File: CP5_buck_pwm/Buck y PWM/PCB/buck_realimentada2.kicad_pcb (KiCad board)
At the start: 2 copper layers, 95 x 89 mm, 52 parts, among them J1 Vin, J10 Conn_vcc, J11 Conn_vref, J12 Conn_vg1, J13 Conn_vg2, J14 Conn_cuadrada, J15 Conn_sampling, J2 Vout, J3 Conn_gnd, J4 Conn_error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

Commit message: Archivos de salida
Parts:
- moved J11 16.6 mm to (137.1, 137.5)
- moved J4 15.5 mm to (147.3, 139.7)
- moved J12 13.7 mm to (163.4, 91.2)
- moved C13 12.0 mm to (126.0, 76.0), turned to 180 degrees
- moved U4 9.27 mm to (119.9, 69.7), turned to 0 degrees
- moved Rc1 5.30 mm to (165.1, 127.0), turned to -90 degrees
- moved R16 4.27 mm to (160.2, 138.6)
- moved C1 2.92 mm to (157.2, 119.9)
- moved C3 2.92 mm to (157.3, 124.2)
- moved J15 2.34 mm to (177.0, 137.2)
- moved J10 1.17 mm to (152.8, 77.7)
- moved U5 0.59 mm to (129.6, 120.9)
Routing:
- net Net-(U4-ADJ): track 19.5 -> 33.9 mm
- net error: track 67.2 -> 75.3 mm
- net Vin: track 135.3 -> 143.3 mm
- net VCCPWM: track 157.3 -> 153.4 mm
- net Net-(C7-Pad2): track 15.2 -> 11.5 mm
- net sampling: track 24.8 -> 27.2 mm
- net Vref: track 40.4 -> 42.3 mm
- net Vout: track 38.5 -> 39.9 mm
- net Vg1: track 36.8 -> 38.0 mm

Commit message: PCB corregida
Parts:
- removed J5: Conn_pwm, Connector_PinHeader_2.54mm:PinHeader_1x01_P2.54mm_Vertical
- added J7: Conn_01x02_Pin, Connector_PinHeader_2.54mm:PinHeader_1x02_P2.54mm_Vertical, F.Cu at (126.0, 109.5)
- moved C12 10.6 mm to (123.2, 115.8), turned to 0 degrees
- moved C6 4.20 mm to (126.1, 88.8)
- moved J11 2.25 mm to (136.0, 139.5)
- moved U5 1.48 mm to (128.3, 120.2)
- moved U1 1.17 mm to (131.1, 110.1)
- moved R4 0.29 mm to (114.3, 90.2), turned to 0 degrees
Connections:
- C10 pad 2: Net-(U7A-+) -> Net-(U7A--)
- C6 pad 1: Net-(U6B-+) -> Net-(U6B--)
- C7 pad 1: Net-(U7A-+) -> Net-(U7A--)
- R1 pad 1: Net-(U6A--) -> Net-(U6A-+)
- R15 pad 1: Net-(U7A-+) -> Net-(U7A--)
- R17 pad 2: Net-(U7A-+) -> Net-(U7A--)
- R4 pad 2: Net-(U6B-+) -> Net-(U6B--)
- R6 pad 2: Net-(U6A--) -> Net-(U6A-+)
- U1 pad 2: pwm -> Net-(J7-Pin_1)
- U6 pad 2: Net-(U6A--) -> Net-(U2A--)
- U6 pad 3: Net-(U2A--) -> Net-(U6A-+)
- U6 pad 5: Net-(U6B-+) -> Net-(U2A--)
- U6 pad 6: Net-(U2A--) -> Net-(U6B--)
- U7 pad 2: Vref -> Net-(U7A--)
- U7 pad 3: Net-(U7A-+) -> Vref
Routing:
- net Net-(U7A-+): track 22.8 -> 0.00 mm
- net Net-(U7A--): track 0.00 -> 21.7 mm
- net Net-(U6B-+): track 18.0 -> 0.00 mm
- net Net-(U6B--): track 0.00 -> 13.3 mm
- net Net-(U6A--): track 12.3 -> 0.00 mm
- net Net-(U6A-+): track 0.00 -> 10.2 mm
- net Net-(J7-Pin_1): track 0.00 -> 6.43 mm
- net pwm: track 24.1 -> 19.2 mm
- net Net-(U2A--): track 44.1 -> 46.7 mm
- net Vref: track 42.3 -> 43.9 mm
- net Triangular: track 40.4 -> 38.7 mm
- net Net-(U1-VS): track 14.2 -> 12.6 mm
- net HO: track 3.82 -> 4.98 mm
- net Net-(D1-K): track 8.72 -> 9.71 mm
- net GND: track 0.00 -> 0.50 mm

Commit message: Add files via upload
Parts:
- added J5: Conn_gnd2, Connector_PinHeader_2.54mm:PinHeader_1x01_P2.54mm_Vertical, F.Cu at (104.9, 129.8)
- added J8: Conn_vd, Connector_PinHeader_2.54mm:PinHeader_1x01_P2.54mm_Vertical, F.Cu at (171.4, 63.5)
- R1, R10, R12, R15, R16, R17, R2, R3, R5, R7: footprint Resistor_THT:R_Axial_DIN0204_L3.6mm_D1.6mm_P5.08mm_Horizontal -> Resistor_THT:R_Axial_DIN0204_L3.6mm_D1.6mm_P7.62mm_Horizontal
- R4: footprint Resistor_THT:R_Axial_DIN0204_L3.6mm_D1.6mm_P5.08mm_Horizontal -> Potentiometer_THT:Potentiometer_Bourns_3296W_Vertical
- moved J10 21.4 mm to (133.6, 68.3)
- moved J12 19.6 mm to (150.2, 76.7)
- moved C8 11.6 mm to (109.6, 88.6), turned to 180 degrees
- moved J6 8.54 mm to (108.6, 115.5)
- moved M3 6.87 mm to (159.1, 105.8)
- moved J13 6.86 mm to (158.0, 112.2)
- moved C3 6.42 mm to (151.1, 122.6)
- moved C1 6.20 mm to (151.1, 118.9)
- moved Rc1 5.62 mm to (161.6, 122.6), turned to 0 degrees
- moved C5 5.40 mm to (139.7, 63.1), turned to 90 degrees
- moved R16 4.92 mm to (163.5, 142.3)
- moved J15 4.34 mm to (177.0, 141.5)
- moved C4 4.28 mm to (137.5, 101.2), turned to -90 degrees
- moved C13 4.20 mm to (122.5, 73.7), turned to -90 degrees
- moved J7 3.74 mm to (128.5, 112.3), turned to -90 degrees
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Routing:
- net Vd: track 32.1 -> 57.5 mm
- net Vg2: track 35.0 -> 13.2 mm
- net Vout: track 39.9 -> 55.9 mm
- net Net-(U2A--): track 46.7 -> 60.8 mm
- net Triangular: track 38.7 -> 43.8 mm
- net Net-(C7-Pad2): track 11.5 -> 15.8 mm
- net Vg1: track 38.0 -> 42.2 mm
- net VCCPWM: track 153.7 -> 156.6 mm
- net Net-(U6B--): track 13.3 -> 16.1 mm
- net Net-(D1-K): track 9.71 -> 12.1 mm
- net Net-(U1-VS): track 12.6 -> 10.7 mm
- net Net-(U7A--): track 21.7 -> 23.6 mm
- net LO: track 3.78 -> 5.57 mm
- net Net-(J7-Pin_1): track 6.43 -> 4.95 mm
- net Vin: track 143.3 -> 142.1 mm
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
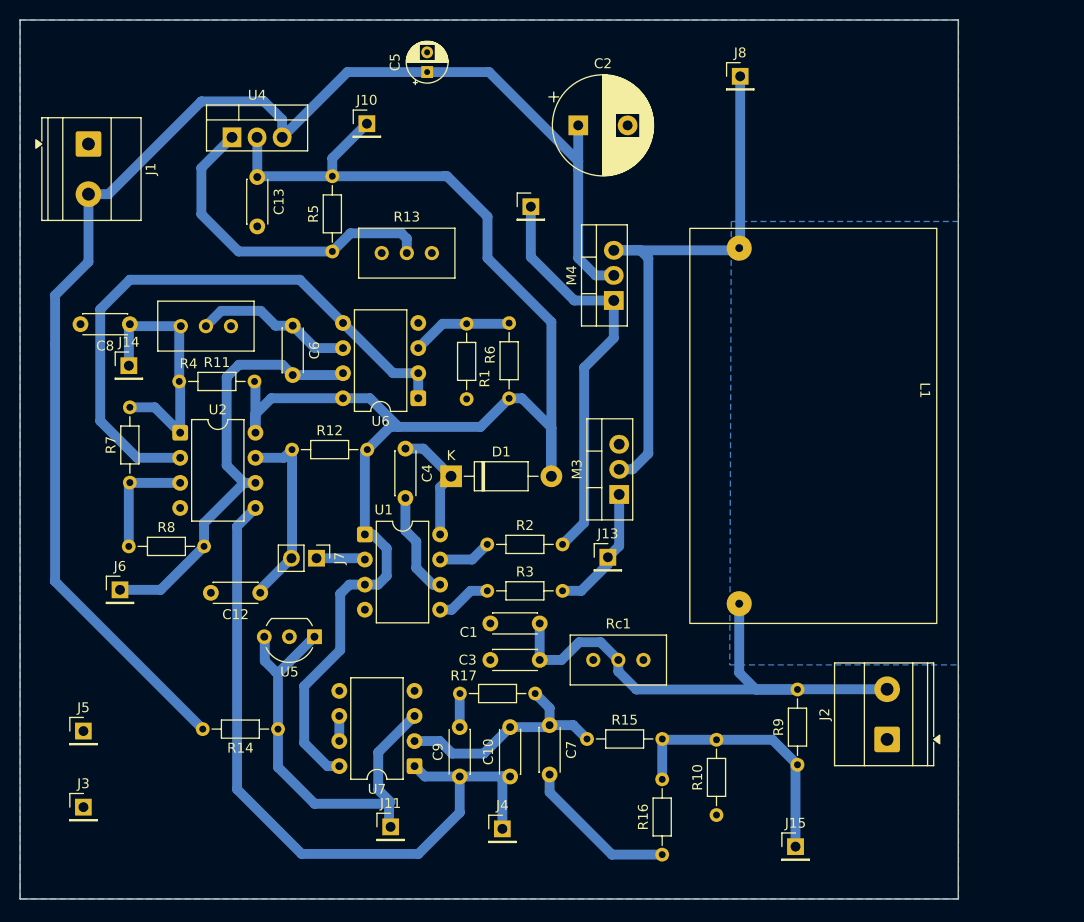
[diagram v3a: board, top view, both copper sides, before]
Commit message: Acomodar pistas gnd y nuevo capacitor
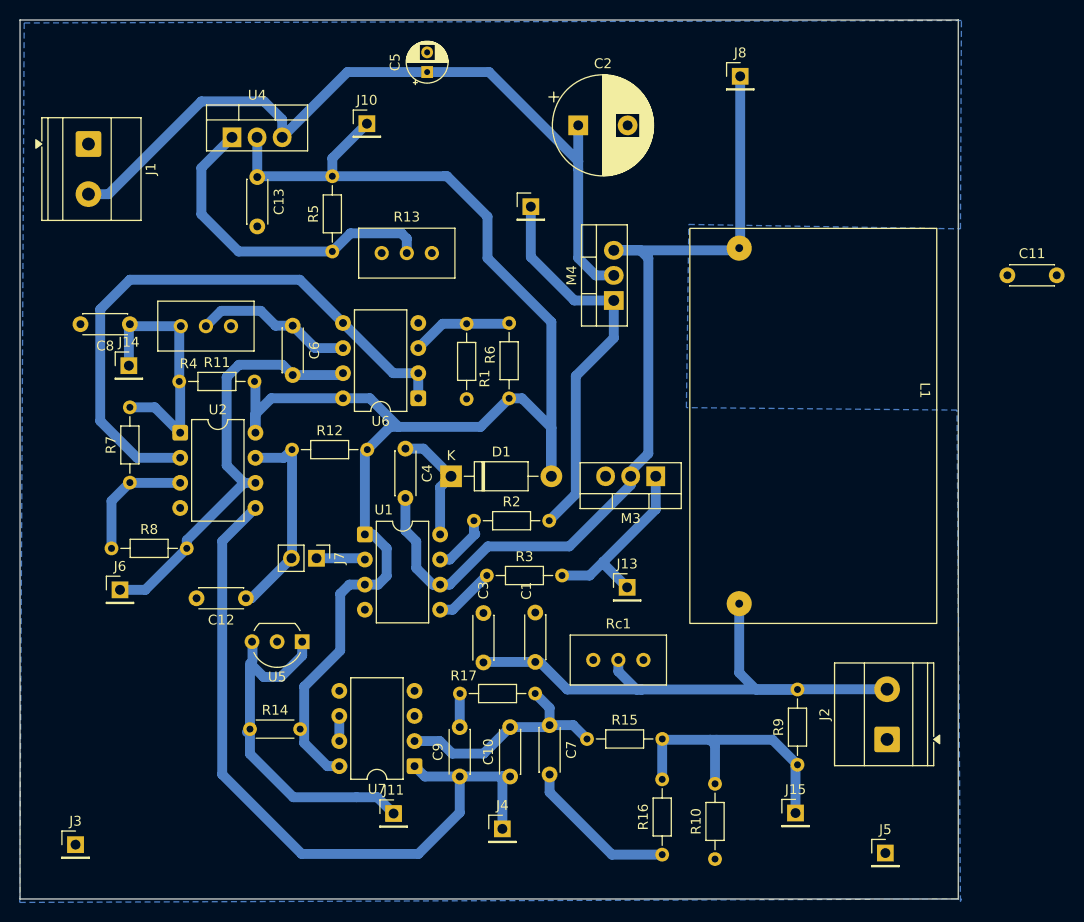
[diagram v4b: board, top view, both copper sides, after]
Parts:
- added C11: 10n, Capacitor_THT:C_Disc_D4.3mm_W1.9mm_P5.00mm, F.Cu at (198.4, 83.7)
- R14: footprint Resistor_THT:R_Axial_DIN0204_L3.6mm_D1.6mm_P7.62mm_Horizontal -> Resistor_THT:R_Axial_DIN0204_L3.6mm_D1.6mm_P5.08mm_Horizontal
- moved J5 82.1 mm to (186.1, 142.2)
- moved C3 5.71 mm to (145.4, 122.8), turned to 90 degrees
- moved R10 4.46 mm to (168.8, 142.8)
- moved M3 4.14 mm to (162.8, 104.0), turned to 180 degrees
- moved C1 3.93 mm to (150.7, 122.8), turned to 90 degrees
- moved J3 3.88 mm to (104.1, 141.3)
- moved J13 3.62 mm to (159.9, 115.2)
- moved J15 3.40 mm to (177.0, 138.1)
- moved R14 2.84 mm to (121.8, 129.6), turned to 0 degrees
- moved R2 2.75 mm to (144.4, 108.5)
- moved R8 1.76 mm to (107.7, 111.3)
- moved C12 1.55 mm to (121.3, 116.3)
- moved R3 1.55 mm to (145.7, 114.0)
- moved J11 1.38 mm to (136.3, 138.2)
- moved U5 1.34 mm to (127.0, 120.8)
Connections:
- C4 pad 2: Net-(U1-VS) -> Vd
- R14 pad 2: Vin -> VCCPWM
- U1 pad 6: Net-(U1-VS) -> Vd
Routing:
- net Vin: track 142.1 -> 80.3 mm
- net Vd: track 57.5 -> 91.1 mm
- net Net-(U1-VS): track 10.7 -> 0.00 mm
- net Vref: track 43.9 -> 35.9 mm
- net Vg2: track 13.2 -> 19.2 mm
- net Vout: track 55.9 -> 60.0 mm
- net Vg1: track 42.2 -> 40.3 mm
- net pwm: track 20.0 -> 21.5 mm
- net sampling: track 27.2 -> 28.5 mm
- net error: track 75.3 -> 76.6 mm
- net Net-(U2A-+): track 11.6 -> 12.5 mm
- net Triangular: track 43.8 -> 42.9 mm
- net HO: track 5.41 -> 6.03 mm
- net LO: track 5.57 -> 6.16 mm

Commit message: PCB en proceso
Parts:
- removed Rc1: 50, Potentiometer_THT:Potentiometer_Bourns_3296W_Vertical
- moved C11 77.9 mm to (130.6, 122.0)
- moved C1 12.0 mm to (162.2, 125.7)
- moved C3 12.0 mm to (157.0, 125.8)
- moved R13 5.72 mm to (135.0, 79.1), turned to 180 degrees
- moved R17 5.30 mm to (143.0, 120.7)
- moved M3 3.03 mm to (162.0, 101.1), turned to 90 degrees
- moved R6 2.36 mm to (146.1, 94.7)
- moved R1 1.60 mm to (143.2, 87.0)
- moved L1 0.75 mm to (192.1, 78.8)
- moved C4 0.70 mm to (137.5, 101.9)
- moved D1 0.07 mm to (142.1, 104.0)
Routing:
- net Vout: track 60.0 -> 40.8 mm
- net Vref: track 35.9 -> 45.7 mm
- net Net-(U7A--): track 23.6 -> 28.9 mm
- net Net-(C9-Pad2): track 3.41 -> 8.70 mm
- net VCCPWM: track 156.6 -> 152.8 mm
- net Vg2: track 19.2 -> 21.6 mm
- net Net-(U4-ADJ): track 33.9 -> 32.2 mm
- net Net-(U6A-+): track 10.2 -> 9.18 mm
